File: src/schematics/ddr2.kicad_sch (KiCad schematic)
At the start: 23 parts, among them U11 IS43DR86400E

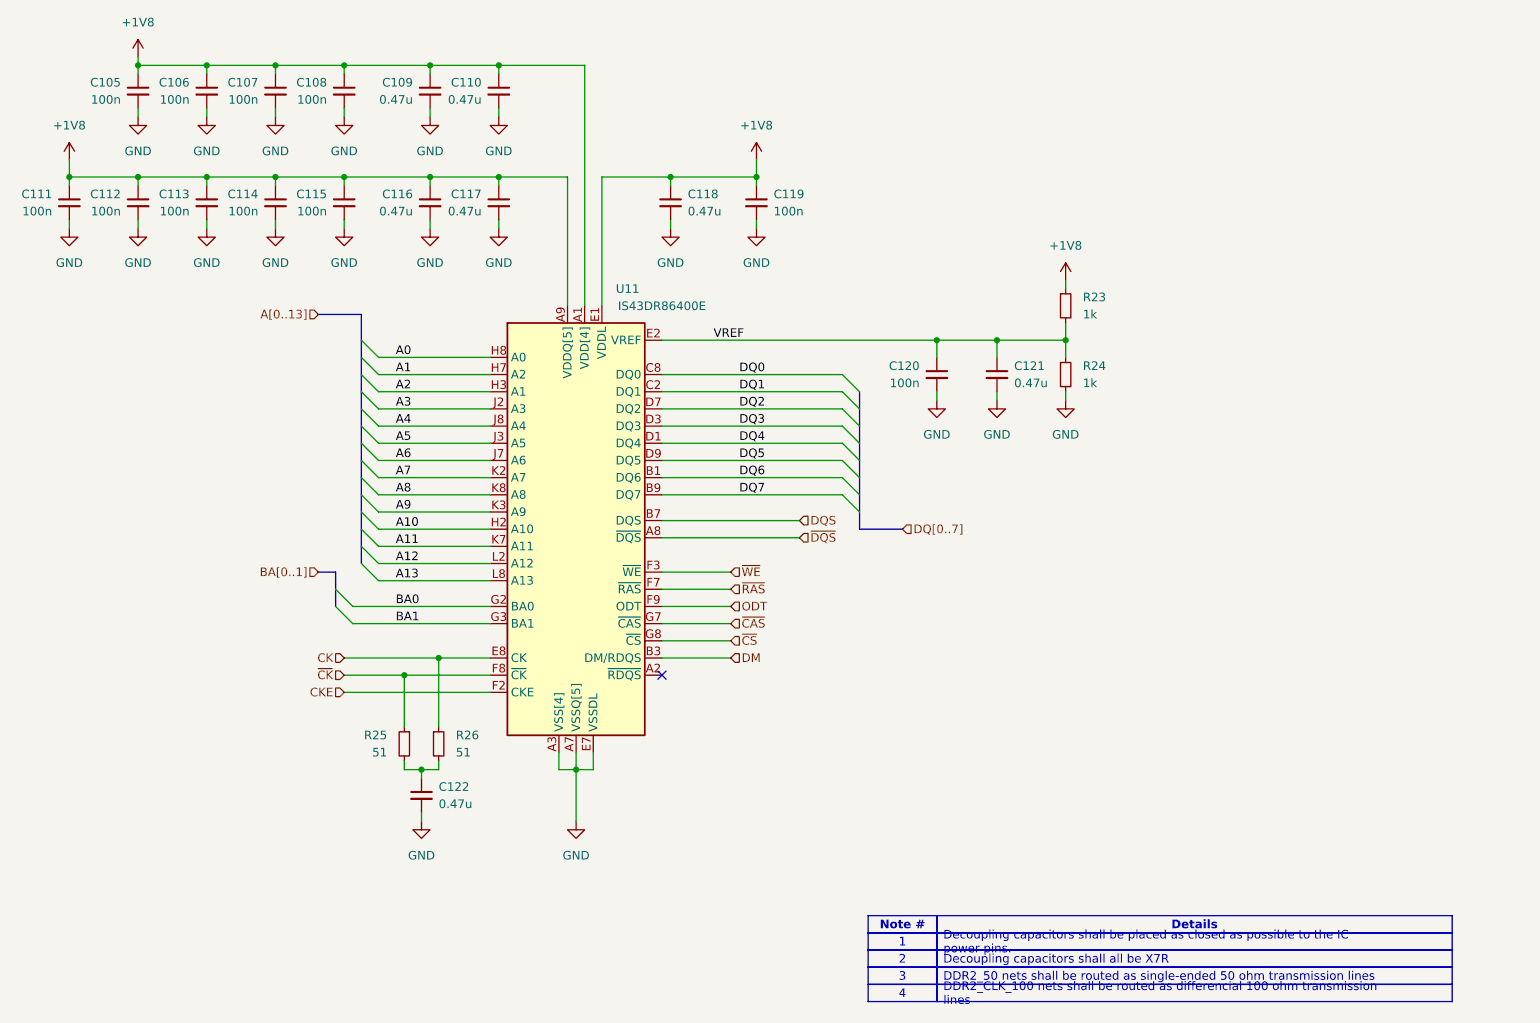
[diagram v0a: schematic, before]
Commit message: Start routing DDR2 data lanes
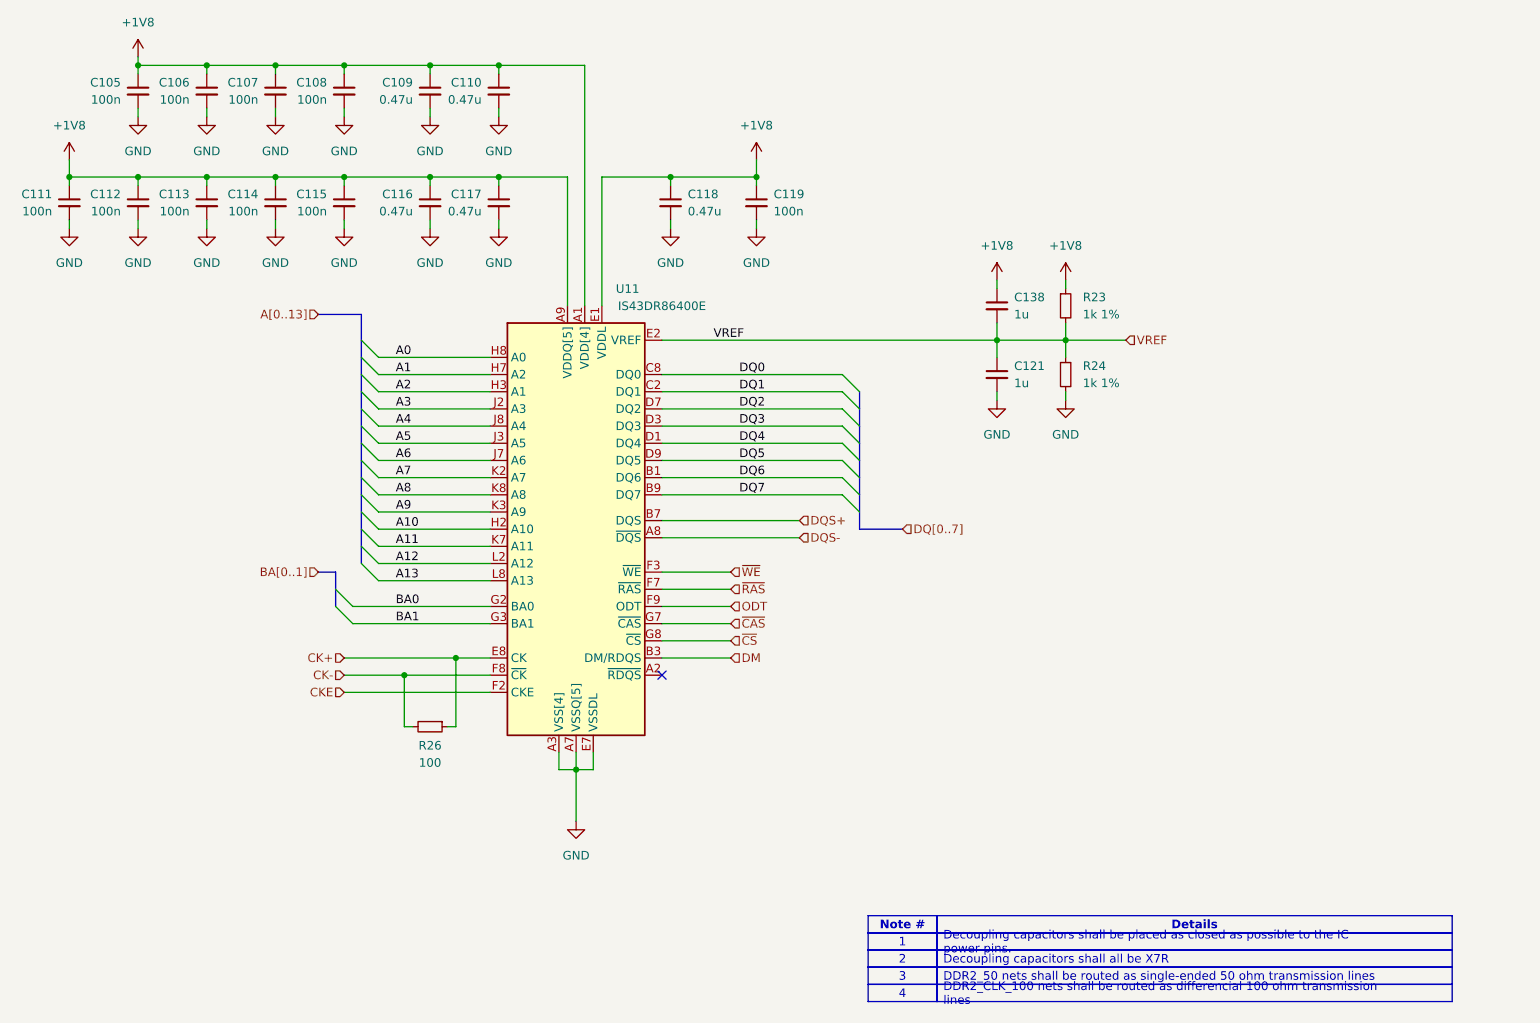
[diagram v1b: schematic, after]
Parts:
- removed C120: 100n, Capacitor_SMD:C_0201_0603Metric, symbol Device:C_Small
- removed C122: 0.47u, Capacitor_SMD:C_0402_1005Metric, symbol Device:C_Small
- removed R25: 51, Resistor_SMD:R_0603_1608Metric, symbol Device:R_Small
- added C138: 1u, Capacitor_SMD:C_0201_0603Metric, symbol Device:C_Small
- C121: value 0.47u -> 1u
- R23, R24: value 1k -> 1k 1%; footprint Resistor_SMD:R_0603_1608Metric -> Resistor_SMD:R_0201_0603Metric
- R26: value 51 -> 100; footprint Resistor_SMD:R_0603_1608Metric -> Resistor_SMD:R_0201_0603Metric
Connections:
- net ~{CK} is gone; now on net CK-: U11.F8 (~{CK})
- net +1V8: now also C138.1
- net VREF: now also C138.2
- net CK-: now reaches R26.2
- net CK renamed CK+
- net DQS renamed DQS+
- net ~{DQS} renamed DQS-
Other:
- moved on the sheet: R26

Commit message: Route signals from DDR2 to FPGA bank
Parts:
- C121, C138: footprint Capacitor_SMD:C_0201_0603Metric -> Capacitor_SMD:C_0402_1005Metric
- R23, R24: footprint Resistor_SMD:R_0201_0603Metric -> Resistor_SMD:R_0402_1005Metric
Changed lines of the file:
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@@
 		(polyline
 			(pts
-				(xy 166.37 120.65) (xy 166.37 105.41) (xy 168.91 105.41) (xy 168.91 120.65)
+				(xy 130.81 73.66) (xy 130.81 115.57) (xy 133.35 115.57) (xy 133.35 73.66)
 			)
 			(stroke
@@
 		(polyline
 			(pts
-				(xy 130.81 73.66) (xy 130.81 115.57) (xy 133.35 115.57) (xy 133.35 73.66)
+				(xy 166.37 120.65) (xy 166.37 105.41) (xy 168.91 105.41) (xy 168.91 120.65)
 			)
 			(stroke
@@
 			)
 		)
-		(property "Footprint" "Resistor_SMD:R_0201_0603Metric"
+		(property "Footprint" "Resistor_SMD:R_0402_1005Metric"
 			(at 222.25 67.31 0)
 			(effects
@@
 			)
 		)
-		(property "Footprint" "Capacitor_SMD:C_0201_0603Metric"
+		(property "Footprint" "Capacitor_SMD:C_0402_1005Metric"
 			(at 212.09 67.31 0)
 			(effects
@@
 			)
 		)
-		(property "Footprint" "Capacitor_SMD:C_0201_0603Metric"
+		(property "Footprint" "Capacitor_SMD:C_0402_1005Metric"
 			(at 212.09 77.47 0)
 			(effects
@@
 			)
 		)
-		(property "Footprint" "Resistor_SMD:R_0201_0603Metric"
+		(property "Footprint" "Resistor_SMD:R_0402_1005Metric"
 			(at 222.25 77.47 0)
 			(effects
